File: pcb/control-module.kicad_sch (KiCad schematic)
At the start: 22 parts, among them J1 Screw_Terminal_01x06, J2 Conn_01x07_Pin, J5 Screw_Terminal_01x02, SW1 SW_DIP_x04, U1 TC2185-3.3VxCTTR

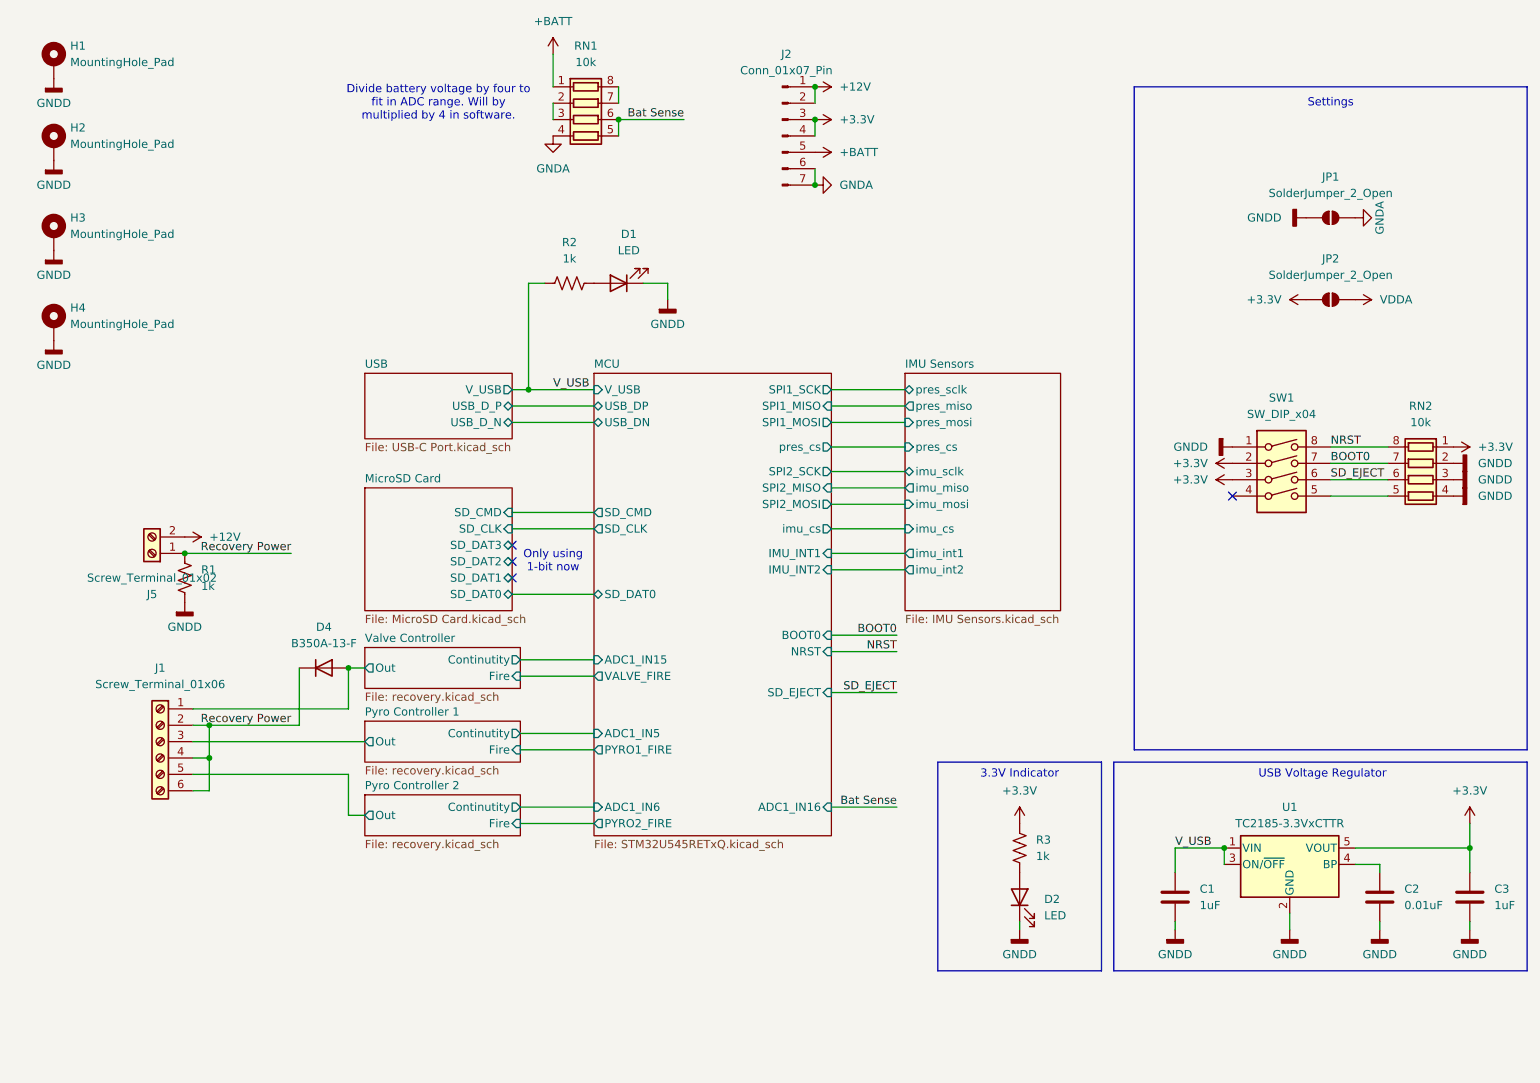
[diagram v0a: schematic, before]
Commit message: Updated Control Module Test bed schematics
Added Test points for Pyro controllers, Micro SD, and USB-C

Connected VDDUSB to 3.3V and not Vusb
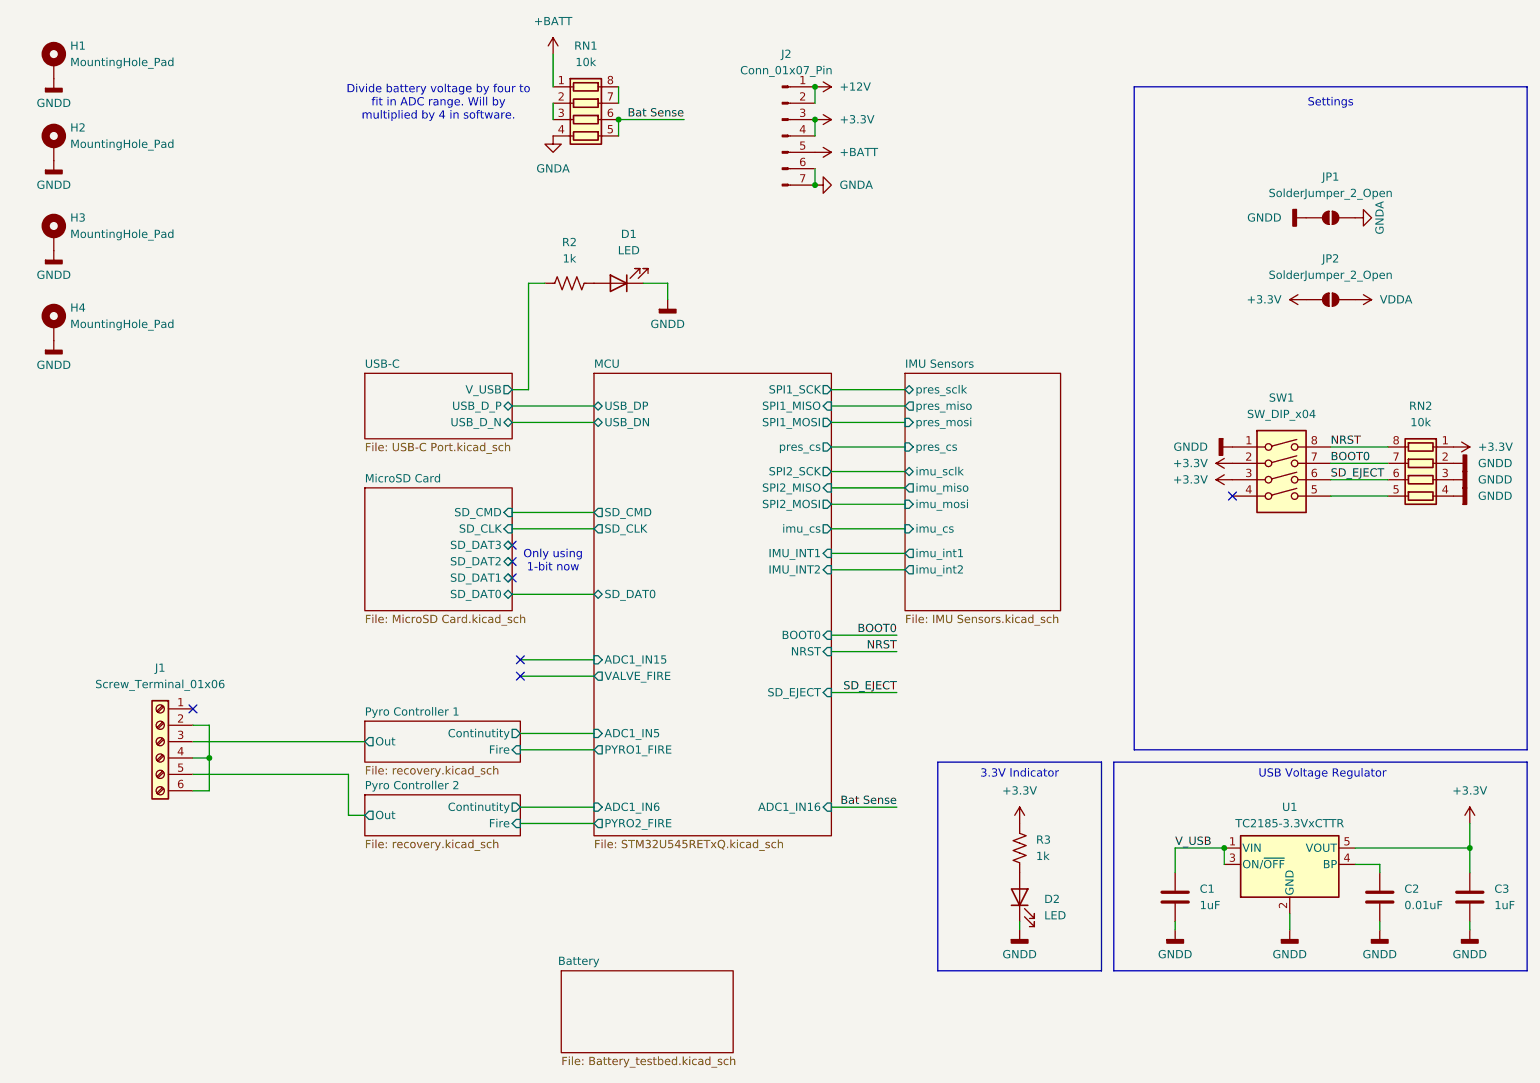
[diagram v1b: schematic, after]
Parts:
- removed D4: B350A-13-F, Diode_SMD:D_SOD-123F, symbol Device:D
- removed J5: Screw_Terminal_01x02, TerminalBlock_Phoenix:TerminalBlock_Phoenix_MPT-0,5-2-2.54_1x02_P2.54mm_Horizontal, symbol Connector:Screw_Terminal_01x02
- removed R1: 1k, Resistor_SMD:R_0603_1608Metric, symbol Device:R_US
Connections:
- net V_USB: no longer R2.1
- net Recovery Power: no longer names the net of J1.2 (Pin_2), J1.4 (Pin_4), J1.6 (Pin_6)
- net Valve Controller/Out: no longer names the net of J1.1 (Pin_1)
- new net USB-C/V_USB: R2.1
- no-connect marks 4 -> 7
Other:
- sheet USB renamed USB-C
- removed sheet Valve Controller
- added sheet Battery (Battery_testbed.kicad_sch)
- sheet MCU ports: added none; removed V_USB
- title: Control Module -> Control Module Testbed

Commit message: Added more testpoints
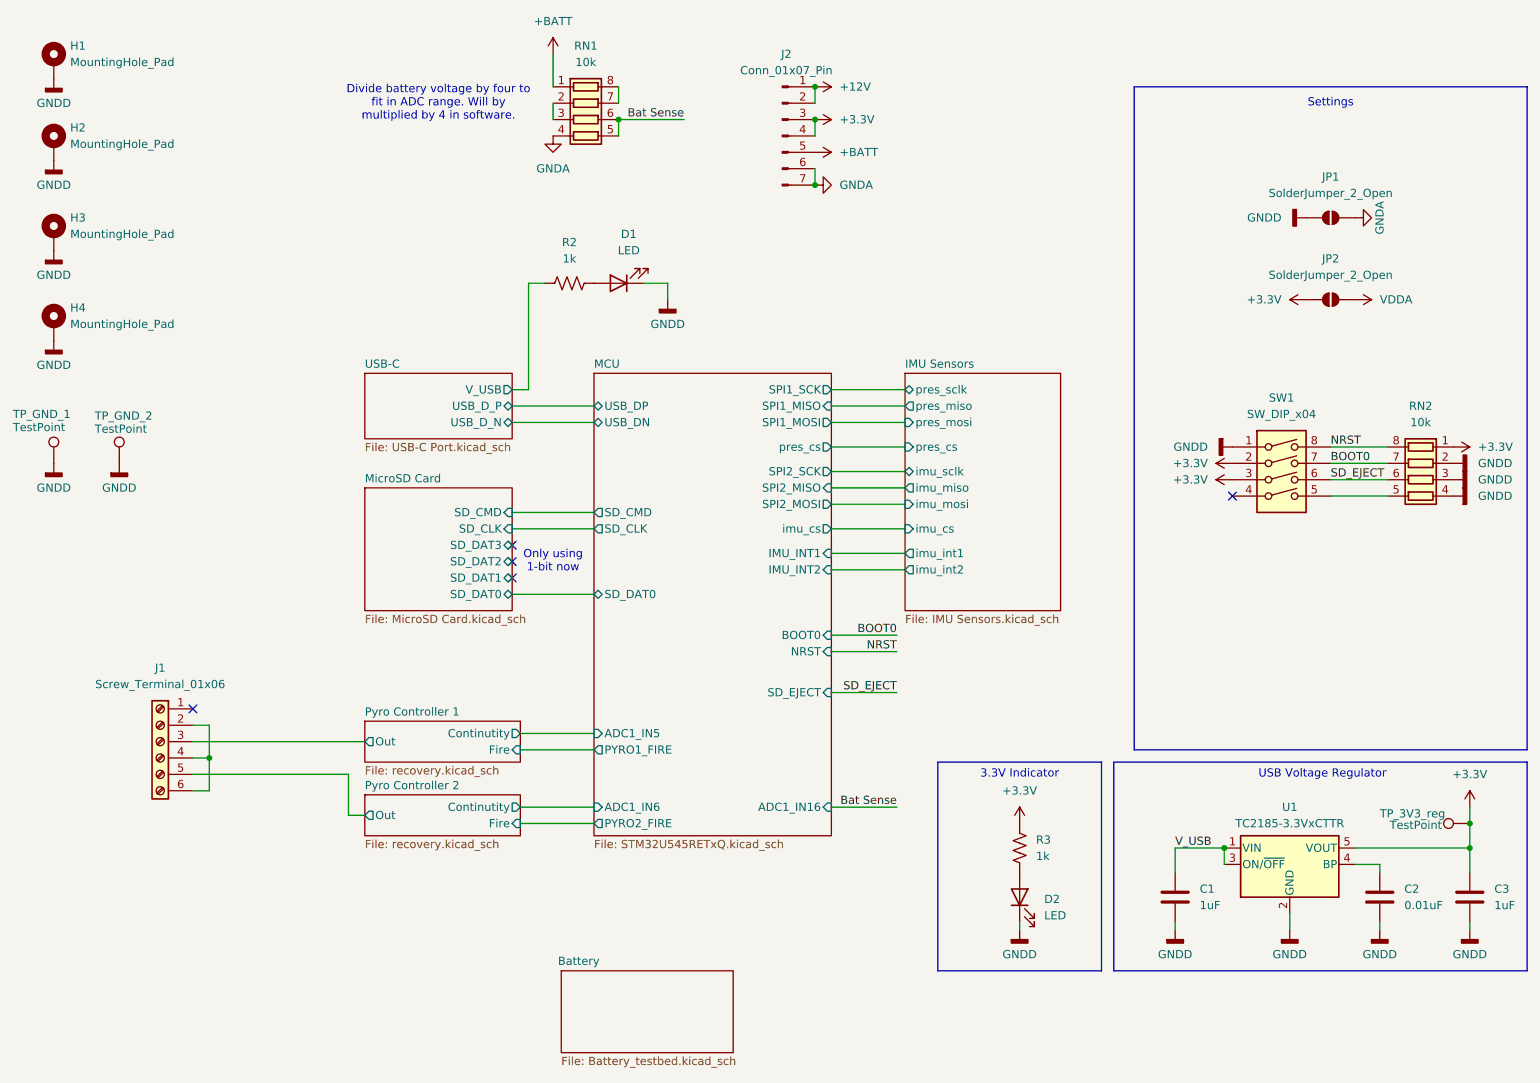
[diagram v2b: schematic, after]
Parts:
- added TP_3V3_reg, TP_GND_1, TP_GND_2: TestPoint, TestPoint:TestPoint_Loop_D2.54mm_Drill1.5mm_Beaded, symbol Connector:TestPoint
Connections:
- net +3.3V: now also TP_3V3_reg.1
- net GNDD: now also TP_GND_1.1, TP_GND_2.1
- no-connect marks 7 -> 5
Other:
- sheet MCU ports: added none; removed ADC1_IN15, VALVE_FIRE
